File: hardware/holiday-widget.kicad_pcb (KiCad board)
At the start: 4 copper layers, 150 x 75 mm, 151 parts, among them J2 UART, J33 Conn_02x05_Odd_Even, J4 BATTERY POWER, J5 VDC POWER, J7 Speaker, Q1 MMBT3906, Q10 MMBT3906, Q11 MMBT3906, Q12 MMBT3906, Q18 MMBT3906, Q19 MMBT3906, Q2 MMBT3906, Q3 MMBT3906, Q4 MMBT3906, Q5 MMBT3906, Q6 MMBT3906, Q7 MMBT3906, Q8 MMBT3906, Q9 MMBT3906, SW1 SW_Push, SW4 SW_Push, U1 STM32L072RBTx, U2 TPS61200DRC, U3 LIS3DH, U4 IMP23ABSU, U6 VCNL_4020, U7 PAM8302AAD, U8 OPA355NA

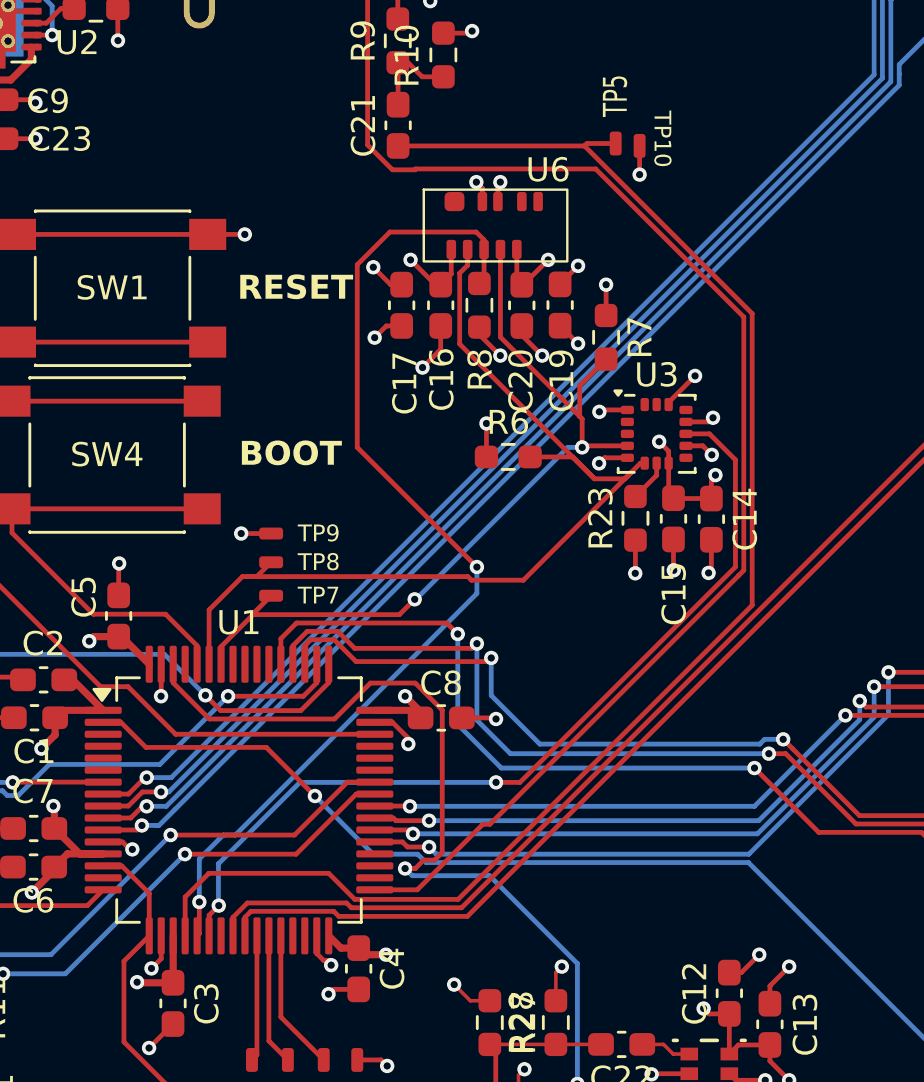
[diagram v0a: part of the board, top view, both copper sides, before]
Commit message: [Hardware] Replace LISDH Motion Sensor with LSM6DSM
Change motion sensor to an accelerometer + gyro unit. Route the second interrupt line to the STM32.
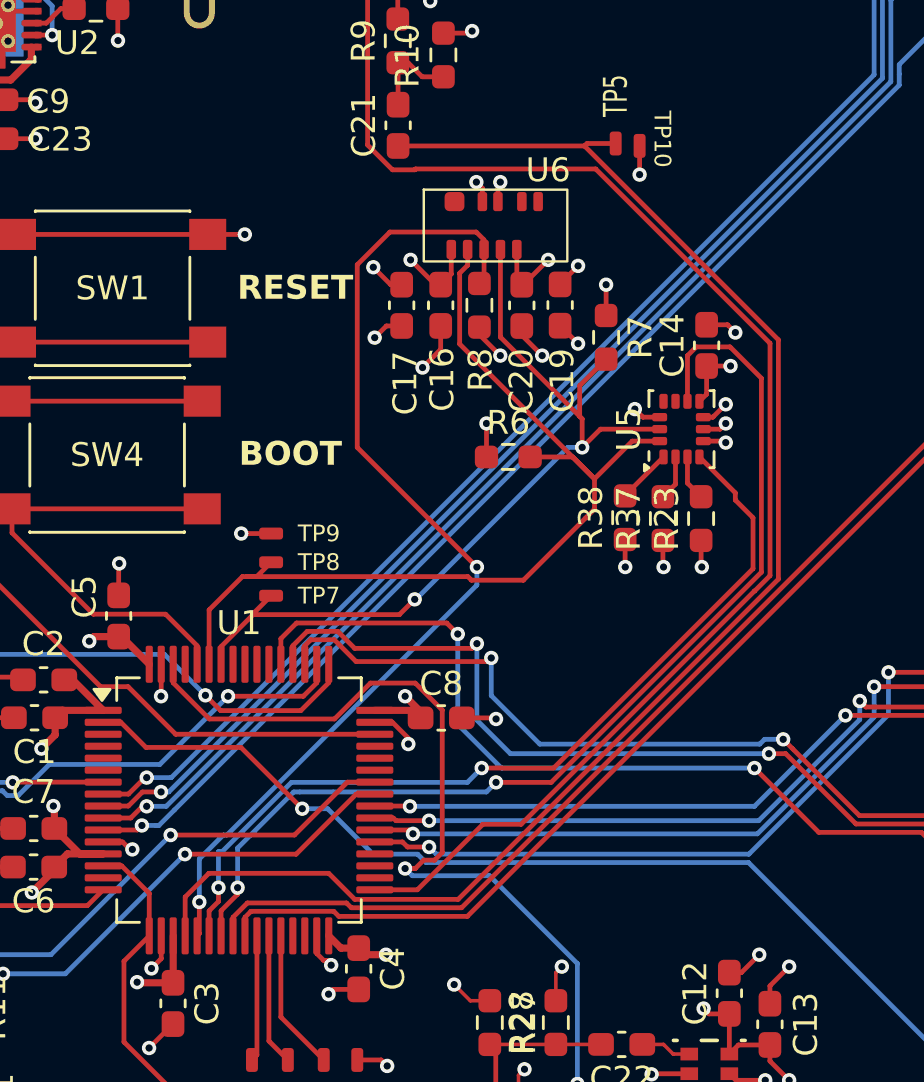
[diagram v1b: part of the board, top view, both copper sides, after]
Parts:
- removed C15: 10u, Capacitor_SMD:C_0603_1608Metric_Pad1.08x0.95mm_HandSolder
- removed U3: LIS3DH, Package_LGA:LGA-16_3x3mm_P0.5mm_LayoutBorder3x5y
- added R37: 0, Resistor_SMD:R_0603_1608Metric_Pad0.98x0.95mm_HandSolder, F.Cu at (163.0, 107.4)
- added R38: 0, Resistor_SMD:R_0603_1608Metric_Pad0.98x0.95mm_HandSolder, F.Cu at (161.4, 107.3)
- added U5: LSM6DSM, Package_LGA:LGA-14_3x2.5mm_P0.5mm_LayoutBorder3x4y, F.Cu at (163.8, 103.6)
- moved C14 7.27 mm to (164.8, 100.1), turned to 90 degrees
- moved R23 2.74 mm to (164.6, 107.4)
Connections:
- U1 pad 22: /Sensors/LIS3DH_INT -> /Sensors/IMU_INT1
- U1 pad 23: unconnected-(U1-PA7-Pad23) -> /Sensors/IMU_INT2
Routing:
- net /Sensors/IMU_INT2: track 0.00 -> 44.4 mm, vias 0 -> 2
- net /Sensors/LIS3DH_INT: track 36.9 -> 0.00 mm, vias 2 -> 0
- net /Sensors/IMU_INT1: track 0.00 -> 36.5 mm, vias 0 -> 2
- net /VDD: track 67.3 -> 63.9 mm, vias 33 -> 32
- net Net-(U5-SDO/SA0): track 0.00 -> 2.29 mm
- net Net-(U5-SDX): track 0.00 -> 1.88 mm
- net /Input and Output/AUDIO_EN: track 57.6 -> 59.3 mm
- net /I2C.SCL: track 34.8 -> 36.5 mm
- net /Input and Output/AUDIO_OUT: track 62.5 -> 63.4 mm
- net /GND: track 109.7 -> 108.8 mm

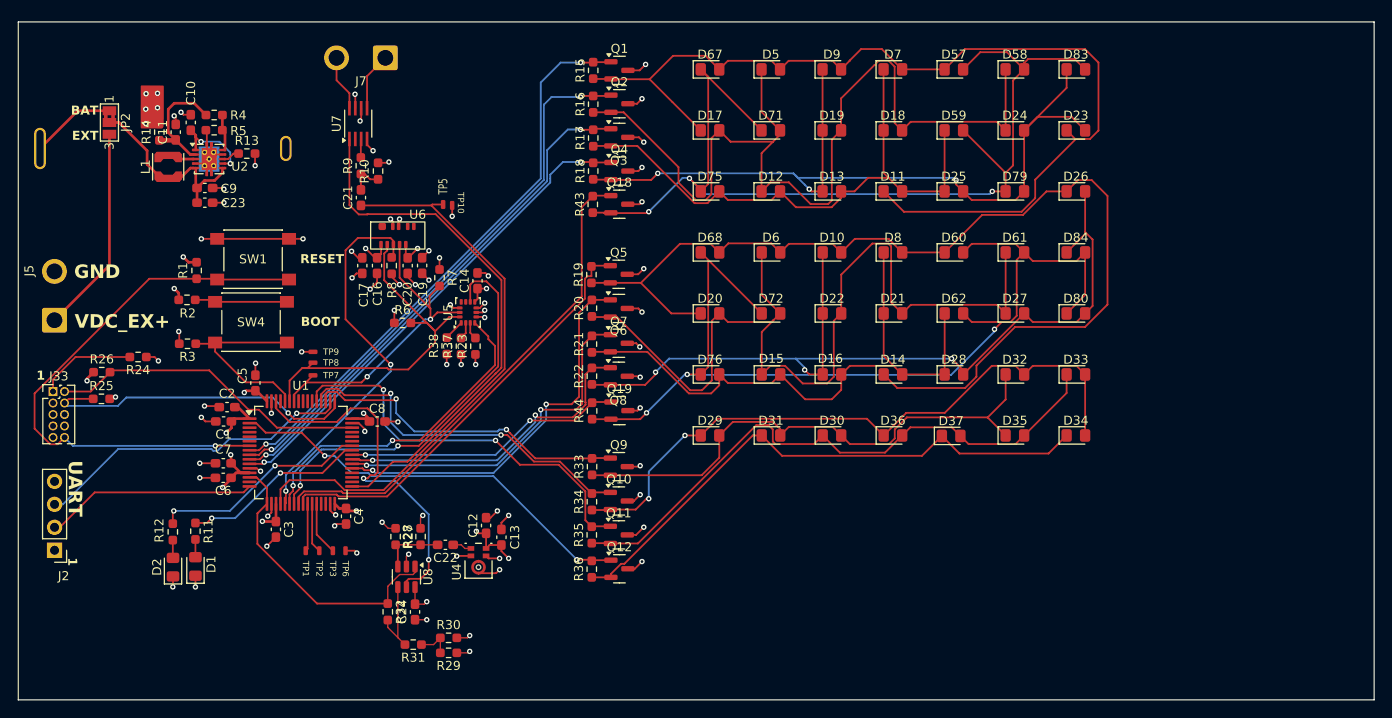
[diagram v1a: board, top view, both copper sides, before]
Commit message: [Hardware] Layout touchups for V2.
Rearrange components mildly to increase density. Decrease footprint size slightly. Fix silkscreen.
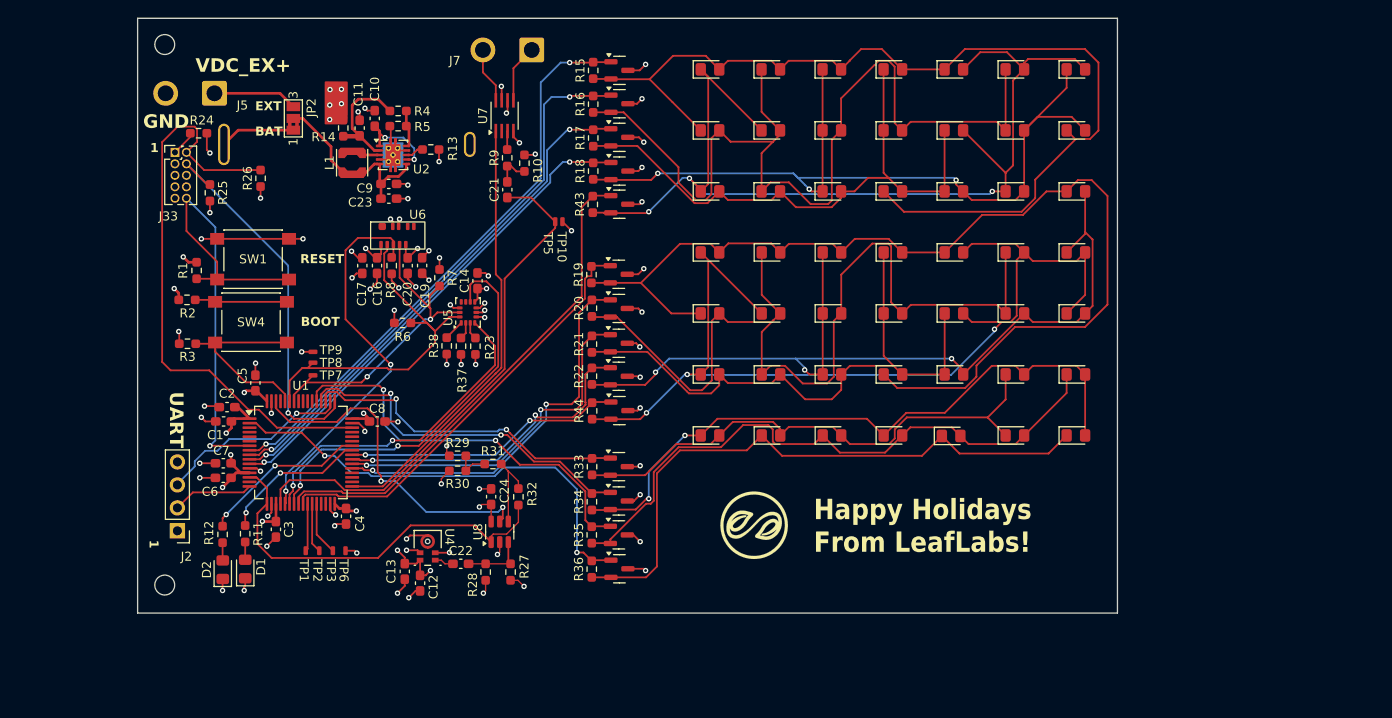
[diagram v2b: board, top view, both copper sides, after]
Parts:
- added G***: LOGO, Leaf_Mechanical:leaf_logo_small, F.Cu at (195.4, 127.2)
- added REF**: MountingHole_2.2mm_M2, MountingHole:MountingHole_2.2mm_M2, F.Cu at (130.2, 133.8)
- added REF**: MountingHole_2.2mm_M2, MountingHole:MountingHole_2.2mm_M2, F.Cu at (130.2, 74.0)
- moved J5 30.7 mm to (135.7, 79.4), turned to 180 degrees
- moved J33 29.7 mm to (131.3, 85.9)
- moved R26 27.7 mm to (140.8, 88.8), turned to 90 degrees
- moved R25 25.8 mm to (135.2, 90.4), turned to -90 degrees
- moved R24 25.6 mm to (133.9, 83.8)
- moved R31 21.8 mm to (166.5, 120.4), turned to 0 degrees
- moved R29 21.8 mm to (162.6, 119.5), turned to 0 degrees
- moved C11 20.4 mm to (151.8, 83.2)
- moved C23 20.4 mm to (155.0, 91.0)
- moved C9 20.4 mm to (155.0, 89.4)
- moved R13 20.4 mm to (159.6, 85.6)
- moved C10 20.4 mm to (153.4, 82.2)
- moved J4 20.4 mm to (150.3, 85.0)
- moved JP2 20.4 mm to (144.4, 82.2), turned to 90 degrees
- moved L1 20.4 mm to (150.9, 87.1)
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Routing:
- net /mcu/SWDIO: track 35.4 -> 65.1 mm
- net /UART.TX: track 23.4 -> 8.97 mm
- net /UART.RX: track 35.8 -> 21.6 mm
- net /VDC_EX: track 23.1 -> 9.34 mm
- net /Audio Amp/AUDIO_OUT: track 32.4 -> 44.1 mm
- net /Input and Output/AUDIO_EN: track 59.3 -> 48.4 mm
- net /mcu/nRST: track 62.5 -> 54.0 mm
- net Net-(J33-Pin_1): track 10.9 -> 2.82 mm
- net /mcu/SWCLK: track 36.0 -> 42.4 mm
- net /Input and Output/LED Output2/CTRL3: track 62.7 -> 68.6 mm
- net /mcu/STAT_LED1: track 24.2 -> 18.5 mm
- net /Input and Output/AUDIO_OUT: track 63.4 -> 57.9 mm
- net /mcu/LED13: track 46.3 -> 51.2 mm
- net /mcu/STAT_LED0: track 20.7 -> 16.4 mm
- net /Audio Amp/AUDIO_AMP_EN: track 40.2 -> 37.6 mm
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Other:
- board size 150 x 75 mm -> 108.4 x 65.8 mm
- board text added: "Happy Holidays From LeafLabs!"
- board text removed: "Holiday Widget V1.0"

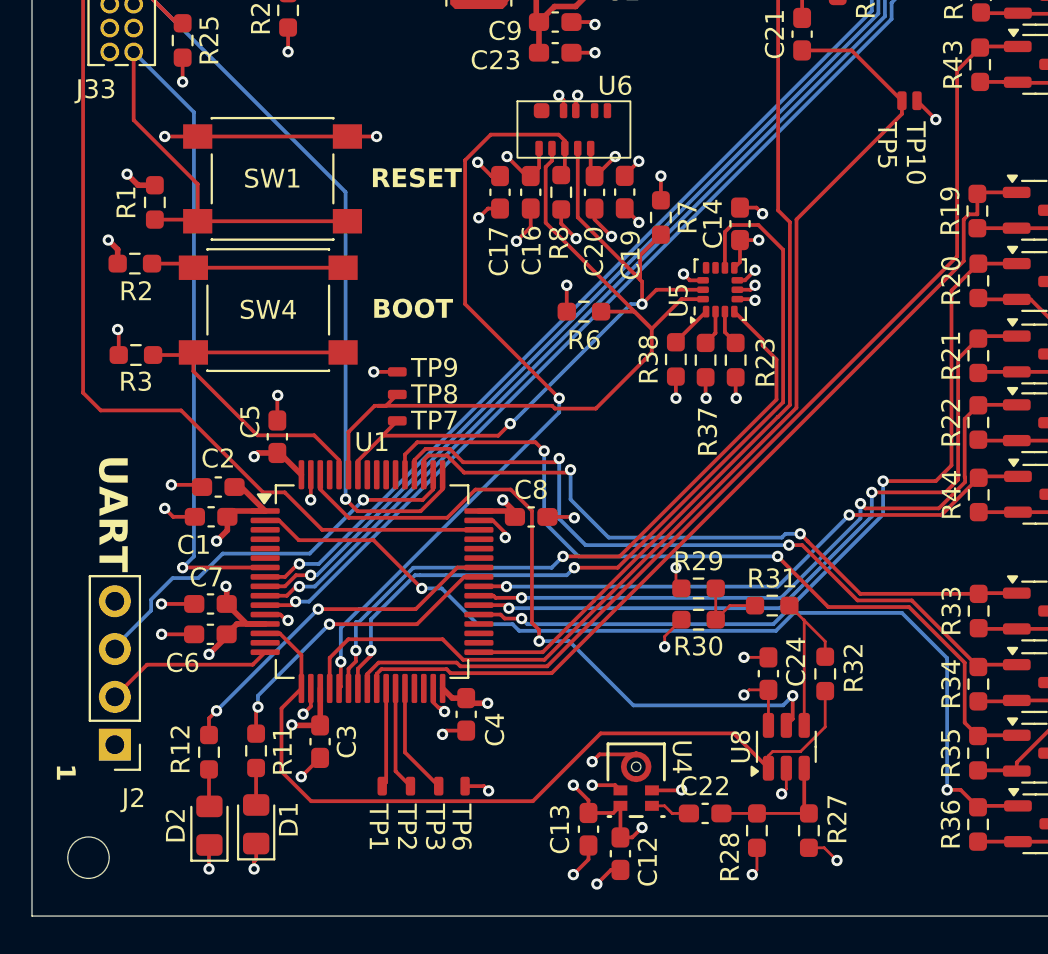
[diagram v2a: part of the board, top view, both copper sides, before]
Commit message: [Hardware] Add ferrite bead to VDDA. Swap schematic symbol for SWD-specific one. Add some notes to MCU pins.
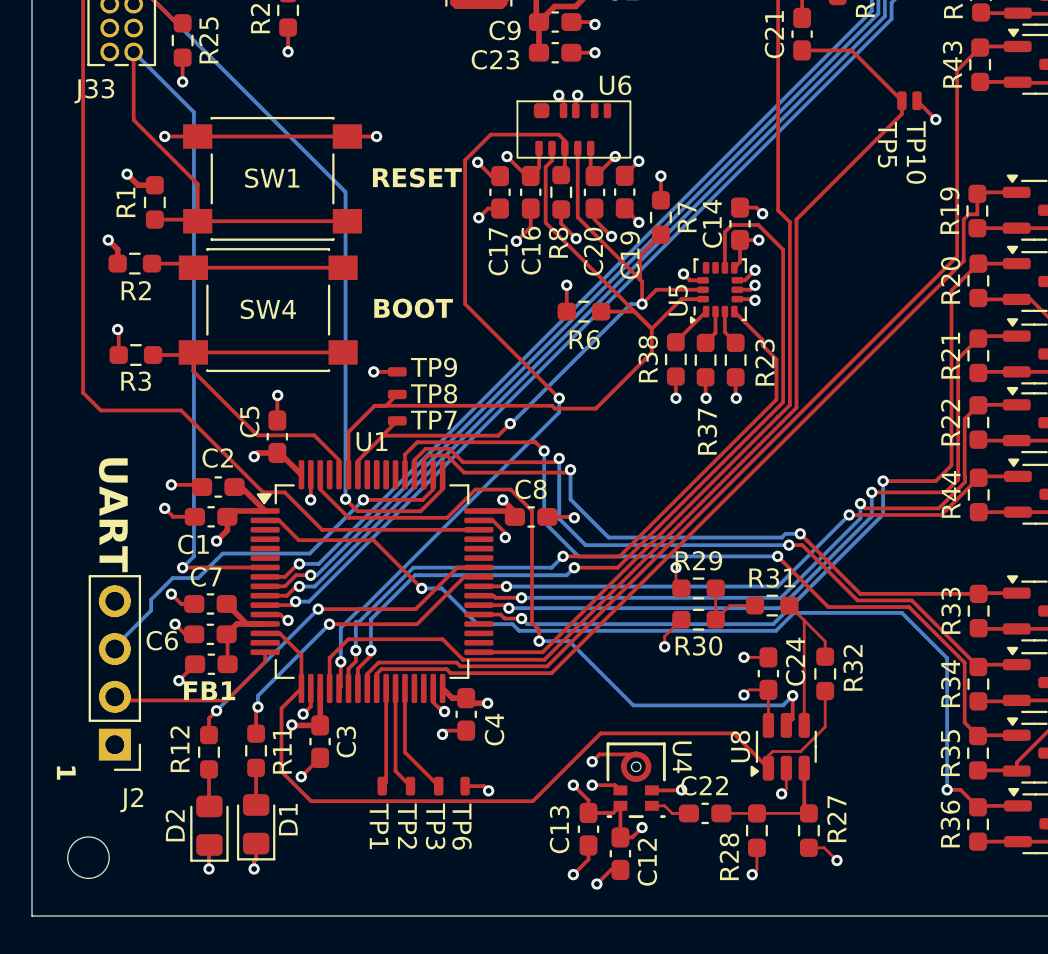
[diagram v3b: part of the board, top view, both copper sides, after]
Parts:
- added FB1: FerriteBead, Capacitor_SMD:C_0603_1608Metric_Pad1.08x0.95mm_HandSolder, F.Cu at (136.7, 123.5)
- J33: value Conn_02x05_Odd_Even -> Conn_ARM_JTAG_SWD_10
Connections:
- C6 pad 1: /VDD -> /mcu/VDDA
- C7 pad 1: /VDD -> /mcu/VDDA
- U1 pad 13: /VDD -> /mcu/VDDA
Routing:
- net /mcu/VDDA: track 0.00 -> 6.37 mm
- net /VDD: track 65.0 -> 59.1 mm, vias 32 -> 31
- net /GND: track 110.1 -> 109.3 mm

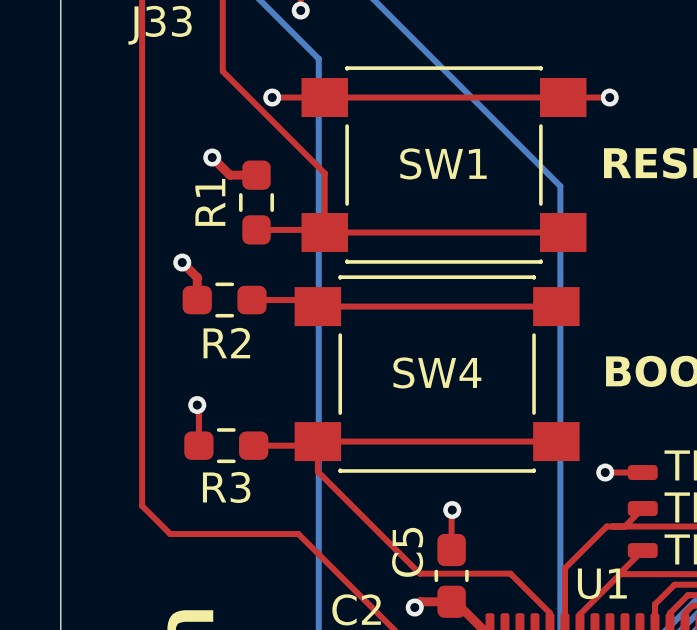
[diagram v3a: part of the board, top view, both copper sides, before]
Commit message: [Hardware] Fix boot button pull-up resistor.
Had an extra resistor, remove it.
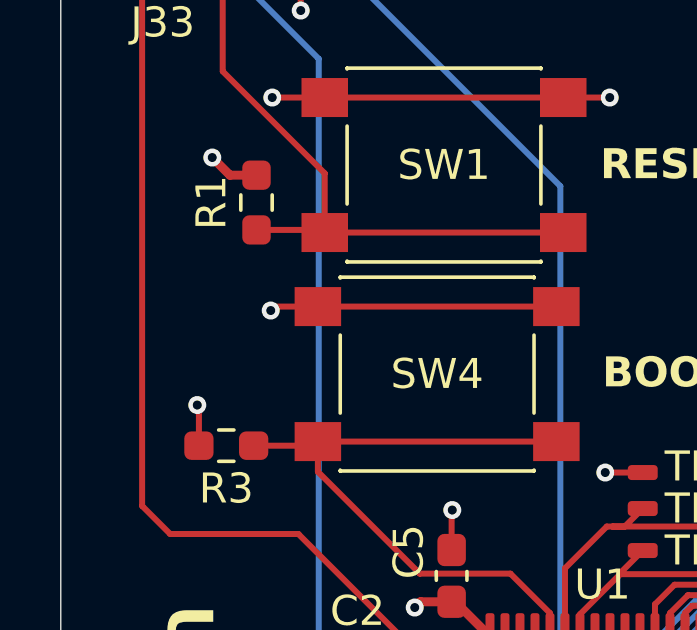
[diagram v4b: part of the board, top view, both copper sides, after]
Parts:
- removed R2: 10k, Resistor_SMD:R_0603_1608Metric_Pad0.98x0.95mm_HandSolder
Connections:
- SW4 pad 2: Net-(R2-Pad2) -> /VDD
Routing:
- net Net-(R2-Pad2): track 10.2 -> 0.00 mm
- net /VDD: track 59.1 -> 67.5 mm

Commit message: [Hardware] Component changes.
* Swap op-amp to similar and cheaper OPA504
* Remove note about tantalum caps (per conversation w Alexa) and plan to replace in BOM with ceramic
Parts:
- U8: value OPA355NA -> OPA504
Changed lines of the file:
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@@
 			)
 		)
-		(property "Value" "OPA355NA"
+		(property "Value" "OPA504"
 			(at 0 2.4 90)
 			(layer "F.Fab")
@@
 			)
 		)
-		(property "Datasheet" "http://www.ti.com/lit/ds/symlink/opa355.pdf"
+		(property "Datasheet" "https://wmsc.lcsc.com/wmsc/upload/file/pdf/v2/lcsc/2303080930_analogysemi-OPA504ASOT236_C5349830.pdf"
 			(at 0 0 90)
 			(unlocked yes)
@@
 			)
 		)
-		(property "Description" "200MHz, CMOS, Operational amplifier, with shutdown, SOT-23-6"
+		(property "Description" "5V, High-Precision, Ultra-Low-Power Operational Amplifiers"
 			(at 0 0 90)
 			(unlocked yes)
@@
 		(sheetname "Sensors")
 		(sheetfile "sensors.kicad_sch")
-		(attr smd)
+		(attr smd exclude_from_pos_files exclude_from_bom)
 		(fp_line
 			(start -0.146267 0.51)

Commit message: [Hardware] Add V2.0 Manufacturing files.
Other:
- board text added: "Holiday Widget v2.0"
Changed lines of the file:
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@@
 			(psnegative no)
 			(psa4output no)
-			(plotreference no)
+			(plotreference yes)
 			(plotvalue no)
-			(plotfptext no)
+			(plotfptext yes)
 			(plotinvisibletext no)
 			(sketchpadsonfab no)
@@
 			(drillshape 0)
 			(scaleselection 1)
-			(outputdirectory "manufacturing/v1.0/gerbers/")
+			(outputdirectory "manufacturing/v2.0/gerbers/")
 		)
 	)
@@
 		(sheetname "Input and Output")
 		(sheetfile "input_output.kicad_sch")
-		(attr exclude_from_pos_files)
+		(attr exclude_from_pos_files exclude_from_bom)
 		(fp_line
 			(start 7.5 1.88)
@@
 		(sheetname "mcu")
 		(sheetfile "mcu.kicad_sch")
-		(attr smd)
+		(attr smd exclude_from_pos_files exclude_from_bom)
 		(fp_text user "${REFERENCE}"
 			(at 0 2.5 180)
@@
 		(sheetname "Root")
 		(sheetfile "holiday-widget.kicad_sch")
-		(attr exclude_from_pos_files)
+		(attr exclude_from_pos_files exclude_from_bom)
 		(fp_line
 			(start 7.5 1.88)
@@
 		(sheetname "Input and Output")
 		(sheetfile "input_output.kicad_sch")
-		(attr smd)
+		(attr smd exclude_from_pos_files exclude_from_bom)
 		(fp_text user "${REFERENCE}"
 			(at 0 2.5 0)
@@
 		(sheetname "Root")
 		(sheetfile "holiday-widget.kicad_sch")
-		(attr through_hole)
+		(attr through_hole exclude_from_pos_files exclude_from_bom)
 		(fp_line
 			(start 1.33 1.27)
@@
 		(sheetname "Input and Output")
 		(sheetfile "input_output.kicad_sch")
-		(attr smd)
+		(attr smd exclude_from_pos_files exclude_from_bom)
 		(fp_text user "${REFERENCE}"
 			(at 0 2.5 180)
@@
 		(sheetname "mcu")
 		(sheetfile "mcu.kicad_sch")
-		(attr smd)
+		(attr smd exclude_from_pos_files exclude_from_bom)
 		(fp_text user "${REFERENCE}"
 			(at 0 2.5 -90)
@@
 		(sheetname "mcu")
 		(sheetfile "mcu.kicad_sch")
-		(attr smd)
+		(attr smd exclude_from_pos_files exclude_from_bom)
 		(fp_text user "${REFERENCE}"
 			(at 0 2.5 180)
@@
 		(sheetname "mcu")
 		(sheetfile "mcu.kicad_sch")
-		(attr smd)
+		(attr smd exclude_from_pos_files exclude_from_bom)
 		(fp_text user "${REFERENCE}"
 			(at 0 2.5 180)
@@
 		(sheetname "mcu")
 		(sheetfile "mcu.kicad_sch")
-		(attr smd)
+		(attr smd exclude_from_pos_files exclude_from_bom)
 		(fp_text user "${REFERENCE}"
 			(at 0 2.5 180)
@@
 		(sheetname "mcu")
 		(sheetfile "mcu.kicad_sch")
-		(attr smd)
+		(attr smd exclude_from_pos_files exclude_from_bom)
 		(fp_text user "${REFERENCE}"
 			(at 0 2.5 -90)
@@
 		(sheetname "mcu")
 		(sheetfile "mcu.kicad_sch")
-		(attr smd)
+		(attr smd exclude_from_pos_files exclude_from_bom)
 		(fp_text user "${REFERENCE}"
 			(at 0 2.5 -90)
@@
 		(sheetname "Root")
 		(sheetfile "holiday-widget.kicad_sch")
-		(attr through_hole)
+		(attr through_hole exclude_from_pos_files exclude_from_bom)
 		(fp_line
 			(start -1.13 -0.76)
@@
 		(sheetname "Sensors")
 		(sheetfile "sensors.kicad_sch")
-		(attr smd exclude_from_pos_files exclude_from_bom)
+		(attr smd)
 		(fp_line
 			(start -0.146267 0.51)
@@
 		(sheetname "Root")
 		(sheetfile "holiday-widget.kicad_sch")
-		(attr through_hole)
+		(attr through_hole exclude_from_pos_files exclude_from_bom)
 		(fp_poly
 			(pts
@@
 		(layer "Edge.Cuts")
 	)
+	(gr_text "Holiday Widget v2.0"
+		(at 158.45 133.5875 -0)
+		(layer "B.SilkS")
+		(effects
+			(font
+				(size 1.5 1.5)
+				(thickness 0.3)
+				(bold yes)
+			)
+			(justify left bottom mirror)
+		)
+	)
 	(gr_text "UART"
